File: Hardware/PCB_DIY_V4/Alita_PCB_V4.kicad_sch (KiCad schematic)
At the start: 21 parts, among them J1 Vss, J2 MUX_header1, J3 MUX_header2, J4 Driver, J5 Buttons, J8 Conn_01x03_Pin, J9 Conn_01x04_Pin, P1 5v_Pins, P2 3.3v_Pins, U1 MUX 4067, U4 ESP32_NODEMCU

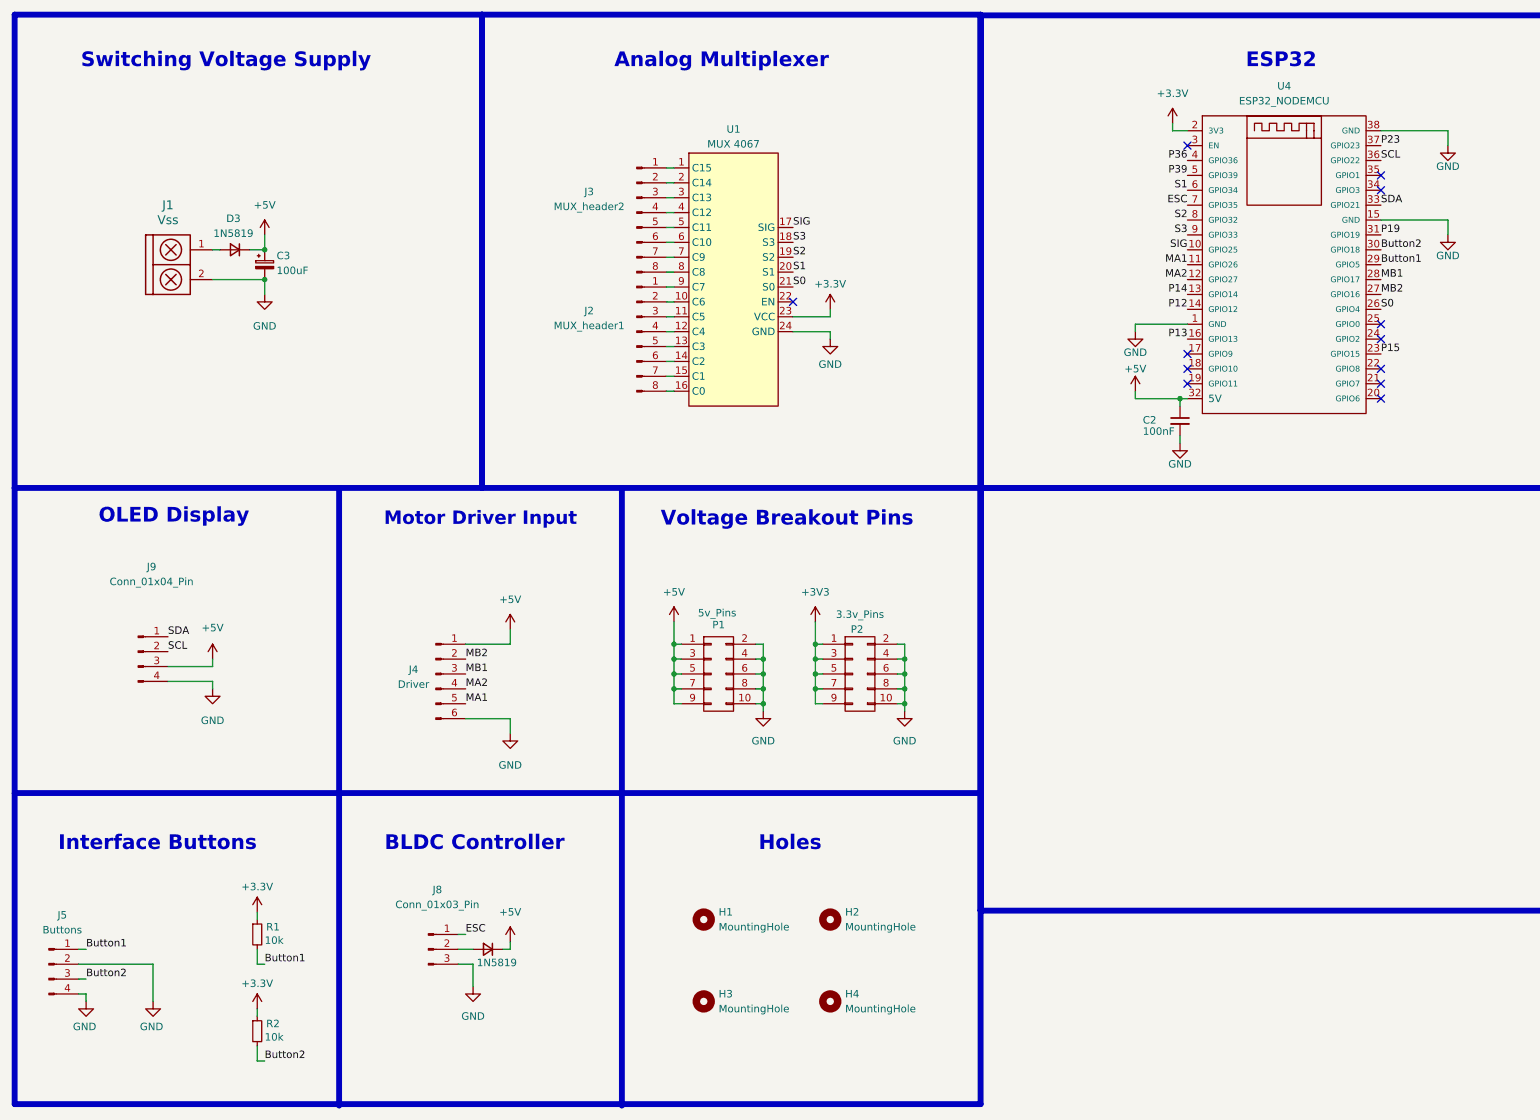
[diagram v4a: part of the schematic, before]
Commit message: Segundo posicionamiento de componentes y ruteo parcial
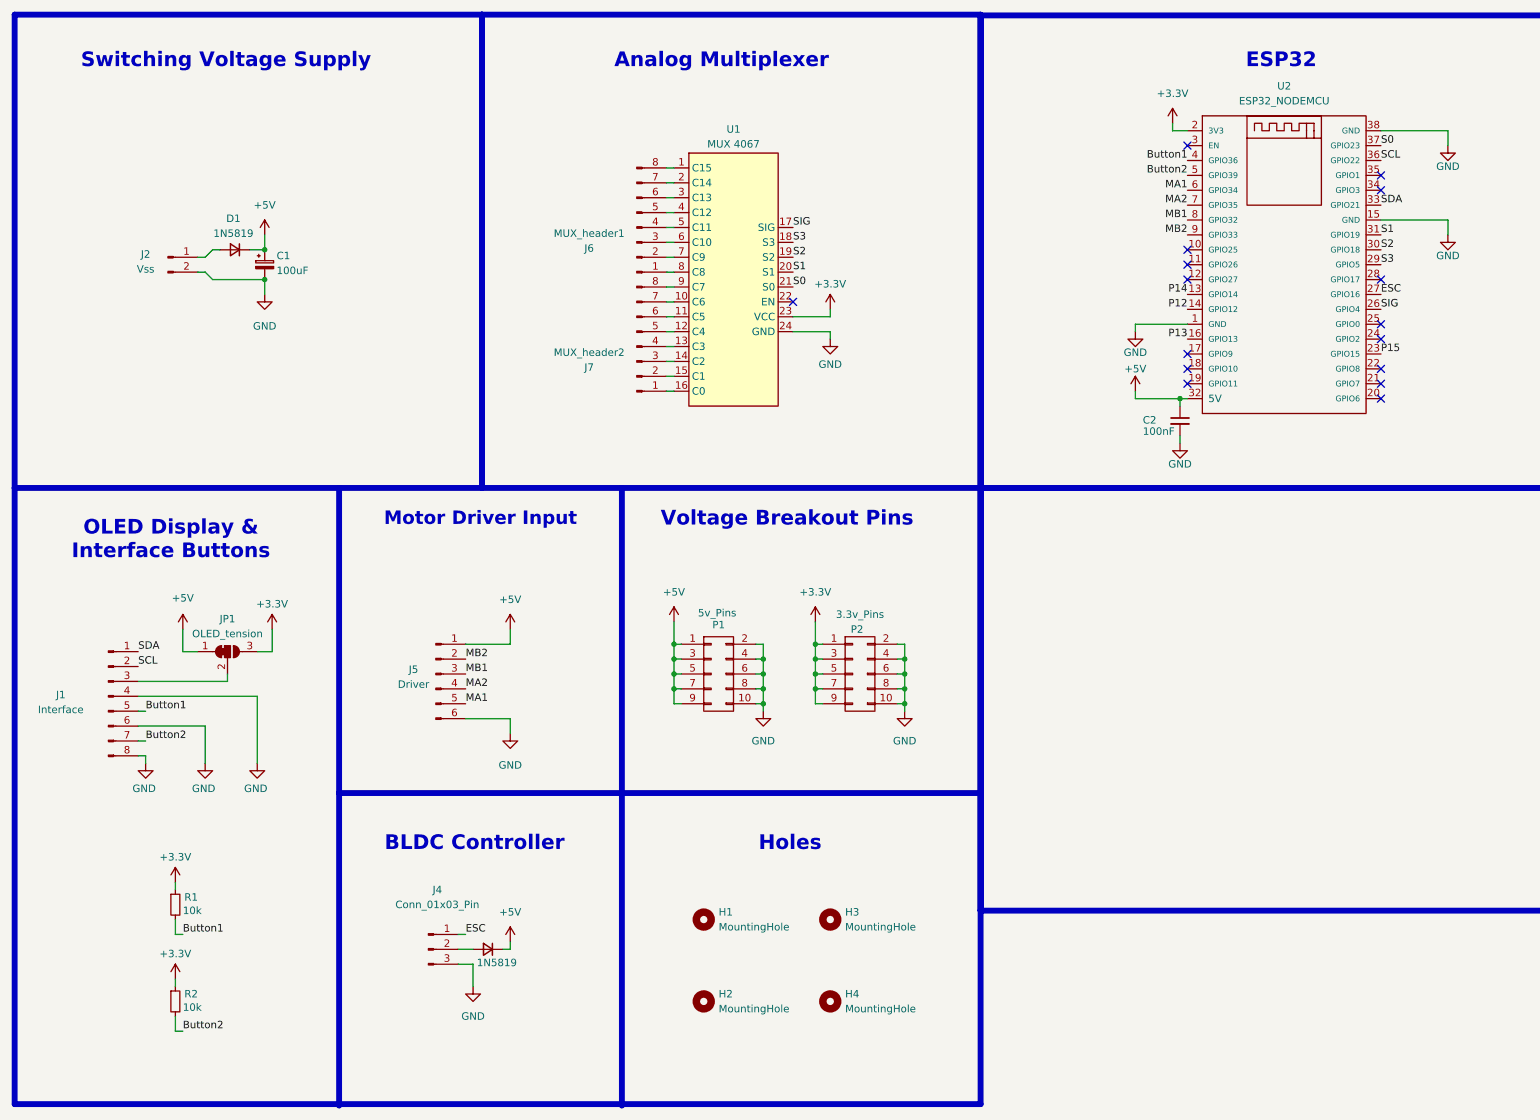
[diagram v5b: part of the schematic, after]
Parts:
- removed J1: Vss, MixLib:Bornera_2_duo, symbol EESTN5:TB_1X2
- removed J5: Buttons, Connector_Molex:Molex_KK-254_AE-6410-04A_1x04_P2.54mm_Vertical, symbol Connector:Conn_01x04_Pin
- removed J9: Conn_01x04_Pin, Connector_Molex:Molex_KK-254_AE-6410-04A_1x04_P2.54mm_Vertical, symbol Connector:Conn_01x04_Pin
- added J1: Interface, Connector_PinHeader_2.54mm:PinHeader_1x08_P2.54mm_Horizontal, symbol Connector:Conn_01x08_Pin
- added J2: Vss, Connector_PinHeader_2.54mm:PinHeader_1x02_P2.54mm_Horizontal, symbol Connector:Conn_01x02_Pin
- added JP1: OLED_tension, MixLib:SolderJumper-3_Big_Bridged, symbol Jumper:SolderJumper_3_Bridged12
- renumbered C3 to C1, D3 to D1, D1 to D2, H3 to H2, H2 to H3, J8 to J4, J4 to J5, J2 to J6, J3 to J7, U4 to U2
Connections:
- net +3V3 is gone; now on net +3.3V: P2.1 (P1), P2.3 (P3), P2.5 (P5), P2.7 (P7), P2.9 (P9)
- net P19 is gone; now on net S1: U2.31 (GPIO19)
- net P23 is gone; now on net S0: U2.37 (GPIO23)
- net P36 is gone; now on net Button1: U2.4 (GPIO36)
- net P39 is gone; now on net Button2: U2.5 (GPIO39)
- net +3.3V: now also JP1.3 (B)
- net +5V: now also JP1.1 (A)
- net Button1: now also J1.5 (Pin_5); no longer U2.29 (GPIO5)
- net Button2: now also J1.7 (Pin_7); no longer U2.30 (GPIO18)
- net ESC: now also U2.27 (GPIO16); no longer U2.7 (GPIO35)
- net GND: now also J1.4 (Pin_4), J1.6 (Pin_6), J1.8 (Pin_8), J2.2 (Pin_2)
- net MA1: now also U2.6 (GPIO34); no longer U2.11 (GPIO26)
- net MA2: now also U2.7 (GPIO35); no longer U2.12 (GPIO27)
- net MB1: now also U2.8 (GPIO32); no longer U2.28 (GPIO17)
- net MB2: now also U2.9 (GPIO33); no longer U2.27 (GPIO16)
- net S0: no longer U2.26 (GPIO4)
- net S1: no longer U2.6 (GPIO34)
- net S2: now also U2.30 (GPIO18); no longer U2.8 (GPIO32)
- net S3: now also U2.29 (GPIO5); no longer U2.9 (GPIO33)
- net SCL: now also J1.2 (Pin_2)
- net SDA: now also J1.1 (Pin_1)
- net SIG: now also U2.26 (GPIO4); no longer U2.10 (GPIO25)
- net at D1.2 (A): now also J2.1 (Pin_1)
- net at J7.1 (Pin_1): now also U1.16 (C0); no longer U1.1 (C15)
- net at J7.2 (Pin_2): now also U1.15 (C1); no longer U1.2 (C14)
- net at J7.3 (Pin_3): now also U1.14 (C2); no longer U1.3 (C13)
- net at J7.4 (Pin_4): now also U1.13 (C3); no longer U1.4 (C12)
- net at J7.5 (Pin_5): now also U1.12 (C4); no longer U1.5 (C11)
- net at J7.6 (Pin_6): now also U1.11 (C5); no longer U1.6 (C10)
- net at J7.7 (Pin_7): now also U1.10 (C6); no longer U1.7 (C9)
- net at J7.8 (Pin_8): now also U1.9 (C7); no longer U1.8 (C8)
- net at J6.2 (Pin_2): now also U1.7 (C9); no longer U1.10 (C6)
- net at J6.3 (Pin_3): now also U1.6 (C10); no longer U1.11 (C5)
- net at J6.4 (Pin_4): now also U1.5 (C11); no longer U1.12 (C4)
- net at J6.5 (Pin_5): now also U1.4 (C12); no longer U1.13 (C3)
- net at J6.6 (Pin_6): now also U1.3 (C13); no longer U1.14 (C2)
- net at J6.7 (Pin_7): now also U1.2 (C14); no longer U1.15 (C1)
- net at J6.8 (Pin_8): now also U1.1 (C15); no longer U1.16 (C0)
- net at J6.1 (Pin_1): now also U1.8 (C8); no longer U1.9 (C7)
- new net: J1.3 (Pin_3), JP1.2 (C)
- no-connect marks 12 -> 16
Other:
- note added: "OLED Display & Interface Buttons"
- note removed: "Interface Buttons"
- note removed: "OLED Display"
- moved on the sheet: J6, J7, R1, R2

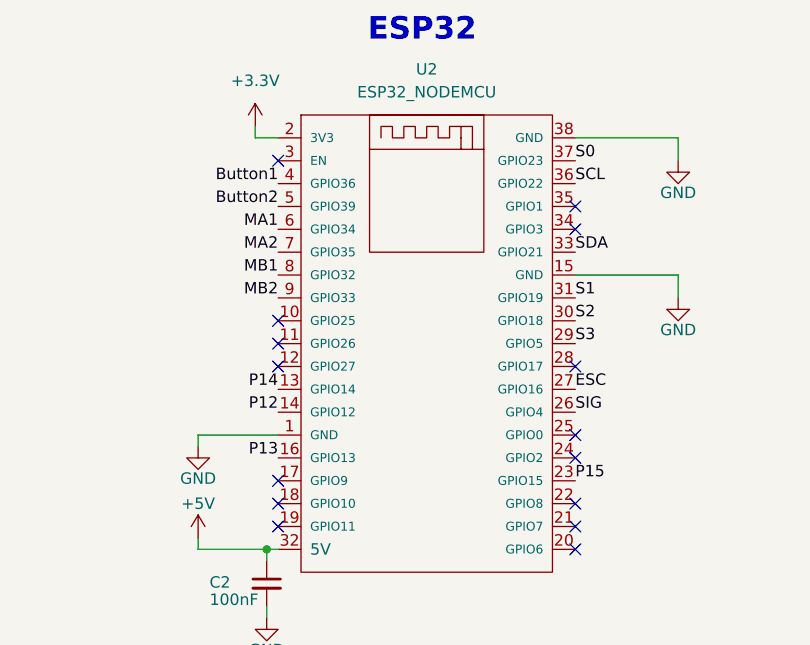
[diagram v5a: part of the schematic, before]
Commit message: PCB_V4: Pinout del ESP32 arreglado
el driver estaba conectado a los pines de input only jeje
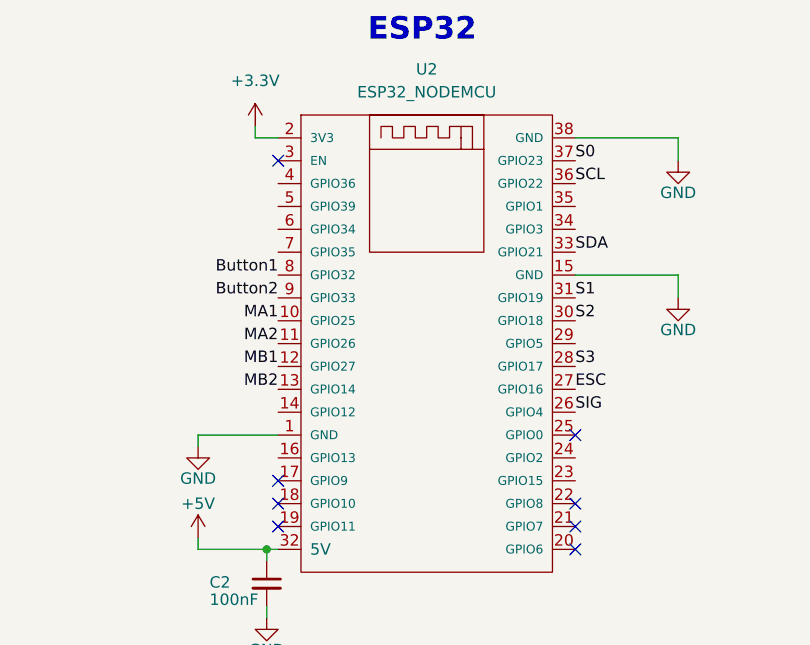
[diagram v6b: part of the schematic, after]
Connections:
- net P14 is gone; now on net MB2: U2.13 (GPIO14)
- net Button1: now also U2.8 (GPIO32); no longer U2.4 (GPIO36)
- net Button2: now also U2.9 (GPIO33); no longer U2.5 (GPIO39)
- net MA1: now also U2.10 (GPIO25); no longer U2.6 (GPIO34)
- net MA2: now also U2.11 (GPIO26); no longer U2.7 (GPIO35)
- net MB1: now also U2.12 (GPIO27); no longer U2.8 (GPIO32)
- net MB2: no longer U2.9 (GPIO33)
- net S3: now also U2.28 (GPIO17); no longer U2.29 (GPIO5)
- net P12: no longer names the net of U2.14 (GPIO12)
- net P13: no longer names the net of U2.16 (GPIO13)
- net P15: no longer names the net of U2.23 (GPIO15)
- no-connect marks 16 -> 9
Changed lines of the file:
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@@
 	)
 	(no_connect
-		(at 245.11 57.15)
+		(at 212.09 34.29)
 	)
 	(no_connect
@@
 	)
 	(no_connect
-		(at 212.09 54.61)
-	)
-	(no_connect
-		(at 245.11 67.31)
-	)
-	(no_connect
 		(at 212.09 74.93)
 	)
 	(no_connect
-		(at 212.09 52.07)
-	)
-	(no_connect
-		(at 212.09 57.15)
-	)
-	(no_connect
-		(at 245.11 41.91)
-	)
-	(no_connect
 		(at 245.11 74.93)
 	)
@@
 	)
 	(no_connect
-		(at 212.09 34.29)
-	)
-	(no_connect
-		(at 245.11 39.37)
-	)
-	(no_connect
 		(at 212.09 69.85)
 	)
@@
 	)
 	(label "MB1"
-		(at 212.09 46.99 180)
+		(at 212.09 57.15 180)
 		(fields_autoplaced yes)
 		(effects
@@
 	)
 	(label "S3"
-		(at 245.11 54.61 0)
+		(at 245.11 57.15 0)
 		(fields_autoplaced yes)
 		(effects
@@
 		)
 	)
-	(label "P14"
-		(at 212.09 59.69 180)
-		(fields_autoplaced yes)
-		(effects
-			(font
-				(size 1.27 1.27)
-			)
-			(justify right bottom)
-		)
-	)
 	(label "MA2"
 		(at 88.9 127 0)
@@
 	)
 	(label "MA1"
-		(at 212.09 41.91 180)
+		(at 212.09 52.07 180)
 		(fields_autoplaced yes)
 		(effects
@@
 	)
 	(label "Button1"
-		(at 212.09 36.83 180)
+		(at 212.09 46.99 180)
 		(fields_autoplaced yes)
 		(effects
@@
 	)
 	(label "MA2"
-		(at 212.09 44.45 180)
+		(at 212.09 54.61 180)
 		(fields_autoplaced yes)
 		(effects
@@
 	)
 	(label "Button2"
-		(at 212.09 39.37 180)
-		(fields_autoplaced yes)
-		(effects
-			(font
-				(size 1.27 1.27)
-			)
-			(justify right bottom)
-		)
-	)
-	(label "P13"
-		(at 212.09 67.31 180)
-		(fields_autoplaced yes)
-		(effects
-			(font
-				(size 1.27 1.27)
-			)
-			(justify right bottom)
-		)
-	)
-	(label "P12"
-		(at 212.09 62.23 180)
+		(at 212.09 49.53 180)
 		(fields_autoplaced yes)
 		(effects
@@
 		)
 	)
-	(label "P15"
-		(at 245.11 69.85 0)
-		(fields_autoplaced yes)
-		(effects
-			(font
-				(size 1.27 1.27)
-			)
-			(justify left bottom)
-		)
-	)
 	(label "MB2"
 		(at 88.9 121.92 0)
@@
 	)
 	(label "MB2"
-		(at 212.09 49.53 180)
+		(at 212.09 59.69 180)
 		(fields_autoplaced yes)
 		(effects

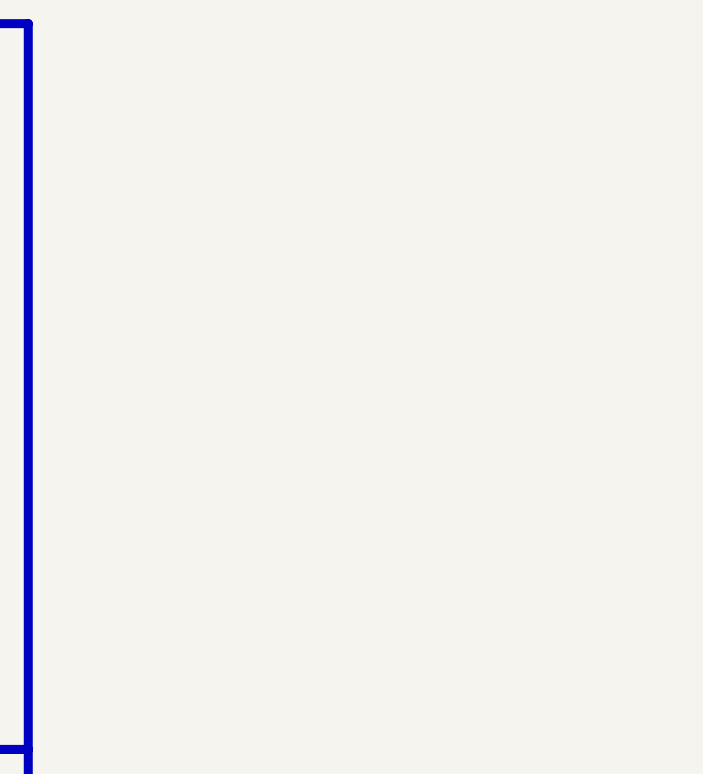
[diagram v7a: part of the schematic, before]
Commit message: Añadi el simbolo arreglado al esquematico y PCB
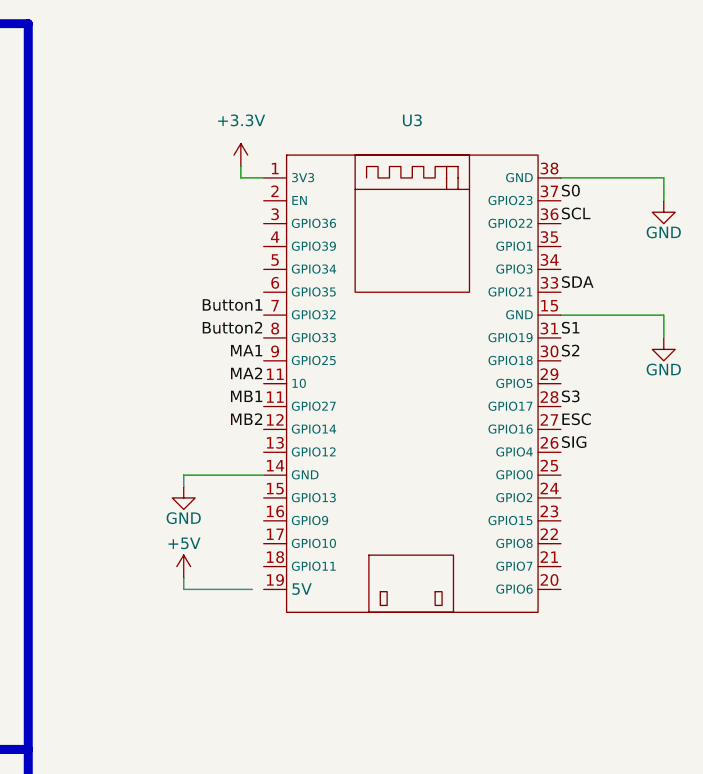
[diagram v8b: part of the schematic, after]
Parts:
- added U3: ~, MixLib:Nodemcu_ESP32S_38pin, symbol MixLib:Nodemcu_ESP32S_38pin
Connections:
- net +3.3V: now also U3.1 (3V3)
- net Button1: now also U3.7 (GPIO32)
- net Button2: now also U3.8 (GPIO33)
- net ESC: now also U3.27 (GPIO16)
- net GND: now also U3.14 (GND), U3.15 (GPIO13), U3.38 (GND)
- net MA1: now also U3.9 (GPIO25)
- net MA2: now also U3.11 (GPIO27)
- net MB1: now also U3.11 (GPIO27)
- net MB2: now also U3.12 (GPIO14)
- net S0: now also U3.37 (GPIO23)
- net S1: now also U3.31 (GPIO19)
- net S2: now also U3.30 (GPIO18)
- net S3: now also U3.28 (GPIO17)
- net SCL: now also U3.36 (GPIO22)
- net SDA: now also U3.33 (GPIO21)
- net SIG: now also U3.26 (GPIO4)
